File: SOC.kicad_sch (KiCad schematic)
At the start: 10 parts, among them J3 TF01-A, J4 CL24CR492, P1 HRO-TYPE-C-31-M-12, SW2 TS-1157-X-A, SW3 TS-1157-X-A, SW4 TS-1157-X-A, SW5 TS-1157-X-A, SW6 TS-1157-X-A, U12 W25Q128JVSIQ, U13 F1C200S

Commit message: dfdfasfasf
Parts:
- removed U13: F1C200S, rlib_ic:QFN-88_EP_10x10_Pitch0.4mm, symbol rlib_ic:F1C200S
- added C47, C48, C49, C50, C? (x12): 100n, symbol rlib_passive:C
- added R? (x4): R, symbol rlib_passive:R
- added U?: F1C200S, rlib_ic:QFN-88_EP_10x10_Pitch0.4mm, symbol rlib_ic:F1C200S
- U12: footprint Package_SO:SOIC-8_5.23x5.23mm_P1.27mm -> rlib_ic:SOIC-8_5.23x5.23mm_P1.27mm
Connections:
- net at SW3.1: now also SW3.2
- net at SW3.3 (K): now also SW3.4 (A)
- net at SW4.1: now also SW4.2
- net at SW4.3 (K): now also SW4.4 (A)
- net LCD_D0: now reaches J4.1 (DB0)
- net LCD_D0: now also U?.49 (PE0/CSI_HSYNC/LCD_D0/TWI2_SCK/TWI2_SCK/UART0_RX/EINTE0)
- net LCD_D1: now reaches J4.2 (DB1)
- net LCD_D1: now also U?.48 (PE1/CSI_VSYNC/LCD_D1/TWI2_SDA/UART0_TX/EINTE1)
- net LCD_D4: now reaches J4.22 (DB4)
- net LCD_D4: now also U?.8 (PD2/LCD_D4/UART1_CTS/EINTD2)
- net LCD_D8: now reaches J4.23 (DB8)
- net LCD_D8: now also U?.47 (PE2/CSI_PCLK/LCD_D8/CLK_OUT/EINTE2)
- net LCD_D9: now reaches J4.24 (DB9)
- net LCD_D9: now also U?.46 (PE3/CSI_D0/LCD_D9/DA_BCLK/RSB_SCK/EINTE3)
- net LCD_D10: now reaches J4.25 (DB10)
- net LCD_D10: now also U?.12 (PD6/LCD_D10/TWI1_SDA/EINTD6)
- net LCD_D12: now reaches J4.26 (DB11)
- net LCD_D12: now also J4.27 (DB12), U?.14 (PD8/LCD_D12/DA_BCLK/EINTD8)
- net LCD_D13: now reaches J4.28 (DB13)
- net LCD_D13: now also U?.15 (PD9/LCD_D13/DA_LRCK/EINTD9)
- net LCD_D14: now reaches J4.29 (DB14)
- net LCD_D14: now also U?.16 (PD10/LCD_D14/DA_IN/EINTD10)
- net LCD_D2: now reaches J4.3 (DB2)
- net LCD_D2: now also U?.6 (PD0/LCD_D2/TWI0_SDA/RSB_SDA/EINTD0)
- net LCD_D15: now reaches J4.30 (DB15)
- net LCD_D15: now also U?.17 (PD11/LCD_D15/DA_OUT/EINTD11)
- net GND: now reaches J4.34 (GND)
- net GND: now also J4.5 (GND), U12.4 (GND), C47.1, C48.2, C49.2, C50.2, C?.2, C?.2, C?.2, C?.2, C?.2, C?.2, C?.2, C?.2, C?.2, C?.2, C?.2, C?.2
- net LCD_D5: now reaches J4.35 (DB5)
- net LCD_D5: now also U?.9 (PD3/LCD_D5/UART1_RX/EINTD3)
- net LCD_D6: now reaches J4.36 (DB6)
- net LCD_D6: now also U?.10 (PD4/LCD_D6/UART1_TX/EINTD4)
- net LCD_D7: now reaches J4.37 (DB7)
- net LCD_D7: now also U?.11 (PD5/LCD_D7/TWI1_SCK/EINTD5)
- net LCD_D3: now reaches J4.4 (DB3)
- net LCD_D3: now also U?.7 (PD1/LCD_D3/UART1_RTS/EINTD1)
- net at SW2.1: now also SW2.2
- net at SW2.3 (K): now also SW2.4 (A)
- net at SW6.1: now also SW6.2
- net at SW6.3 (K): now also SW6.4 (A)
- net at SW5.1: now also SW5.2
- net at SW5.3 (K): now also SW5.4 (A)
- net at P1.A1 (GND), P1.A12 (GND), P1.B1 (GND)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: now also P1.S1 (SHIELD)
- net +3V3: now reaches U12.8 (VCC)
- net +3V3: now also J3.4 (VDD), C47.2, C48.1, C49.1, C50.1, C?.1, C?.1, C?.1, C?.1, R?.1, R?.1, R?.1, R?.1, U?.5 (VCC-IO), U?.67 (UVCC)
- net at J3.1 (DAT2): now also R?.2
- net at J3.2 (DAT3/CD): now also R?.2
- net at J3.7 (DAT0): now also R?.2
- net at J3.8 (DAT1): now also R?.2
- new net +1V1: C?.1, C?.1, C?.1, U?.71 (VDD-CORE)
- new net +2V5: C?.1, C?.1, C?.1, C?.1, C?.1, U?.31 (VCC-DRAM)
- new net BTN1: U?.59 (PC0/SPI0_CLK/SDC1_CLK)
- new net BTN2: U?.60 (PC1/SPI0_CS/SDC1_CMD)
- new net BTN3: U?.61 (PC2/SPI0_MISO/SDC1_D0)
- new net BTN4: U?.62 (PC3/SPI0_MOSI/UART0_TX)
- new net DAC_I2C_SCLK: U?.23 (PD15/LCD_D21/UART2_RTS/TWI2_SCK/EINTD15)
- new net DAC_I2C_SDIN: U?.24 (PD16/LCD_D22/UART2_CTS/TWI2_SDA/EINTD16)
- new net DAC_I2S_BCLK: U?.66 (PA0/TPX1/DA_BCLK/UART1_RTS/SPI1_CS)
- new net DAC_I2S_DIN: U?.63 (PA3/TPY2/IR_RX/DA_OUT/UART1_TX/SPI1_MISO)
- new net DAC_I2S_LRCK: U?.65 (PA1/TPX2/DA_LRCK/UART1_CTS/SPI1_MOSI)
- new net KEYS: U?.79 (LRADC0)
- new net LCD_D11: U?.13 (PD7/LCD_D11/DA_MCLK/EINTD7)
- new net LCD_D16: U?.45 (PE4/CSI_D1/LCD_D16/DA_LRCK/RSB_SDA/EINTE4)
- new net SDC_CLK: U?.56 (PF2/SDC0_CLK/UART0_RX/EINTF2)
- new net SDC_CMD: U?.55 (PF3/SDC0_CMD/DBG_DO/EINTF3)
- new net SDC_D0: U?.57 (PF1/SDC0_D0/DBG_DI/EINTF1)
- new net SDC_D1: U?.58 (PF0/SDC0_D1/DBG_MS/IR_RX/EINTF0)
- new net SDC_D2: U?.53 (PF5/SDC0_D2/DBG_CK/PWM1/EINTF5)
- new net SDC_D3: U?.54 (PF4/SDC0_D3/UART0_TX/EINTF4)
- new net TERM_RX: U?.21 (PD14/LCD_D20/UART2_RX/EINTD14)
- new net TERM_TX: U?.19 (PD13/LCD_D19/UART2_TX/EINTD13)
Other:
- note added: "VCC-IO"
- moved on the sheet: J3, J4, P1, SW2, SW3, SW4, SW5, SW6, U12

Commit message: lradc schematic
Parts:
- added C?: 100n, symbol rlib_passive:C
- added R? (x7): R, symbol rlib_passive:R
- added SW? (x2): KLS7-TS3606, symbol rlib_buttons:KLS7-TS3606
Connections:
- net +3V3: now also R?.1
- net GND: now also J3.6 (VSS), SW2.3 (K), SW2.4 (A), SW3.3 (K), SW3.4 (A), SW4.3 (K), SW4.4 (A), SW5.3 (K), SW5.4 (A), SW6.3 (K), SW6.4 (A), C?.2, SW?.2, SW?.2
- net KEYS: now also SW3.1, SW3.2, R?.1, R?.2
- net SDC_CMD: now also J3.3 (CMD)
- net SDC_D0: now also J3.7 (DAT0), R?.2
- net SDC_D1: now also J3.8 (DAT1), R?.2
- net SDC_D2: now also J3.1 (DAT2), R?.2
- net SDC_D3: now also J3.2 (DAT3/CD), R?.2
- net at SW4.1, SW4.2: now also R?.1, R?.2
- net at SW2.1, SW2.2: now also R?.1, R?.2
- net at SW6.1, SW6.2: now also R?.1, R?.2
- net at SW5.1, SW5.2: now also R?.1, R?.2
- net BTN1: no longer names the net of U?.59 (PC0/SPI0_CLK/SDC1_CLK)
- net BTN2: no longer names the net of U?.60 (PC1/SPI0_CS/SDC1_CMD)
- net BTN3: no longer names the net of U?.61 (PC2/SPI0_MISO/SDC1_D0)
- net BTN4: no longer names the net of U?.62 (PC3/SPI0_MOSI/UART0_TX)
- new net: C?.1, R?.2, SW?.1
- new net: R?.1, R?.2, SW?.1
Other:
- note removed: "VCC-IO"
- moved on the sheet: C48, C49, C50, SW2, SW3, SW4, SW5, SW6

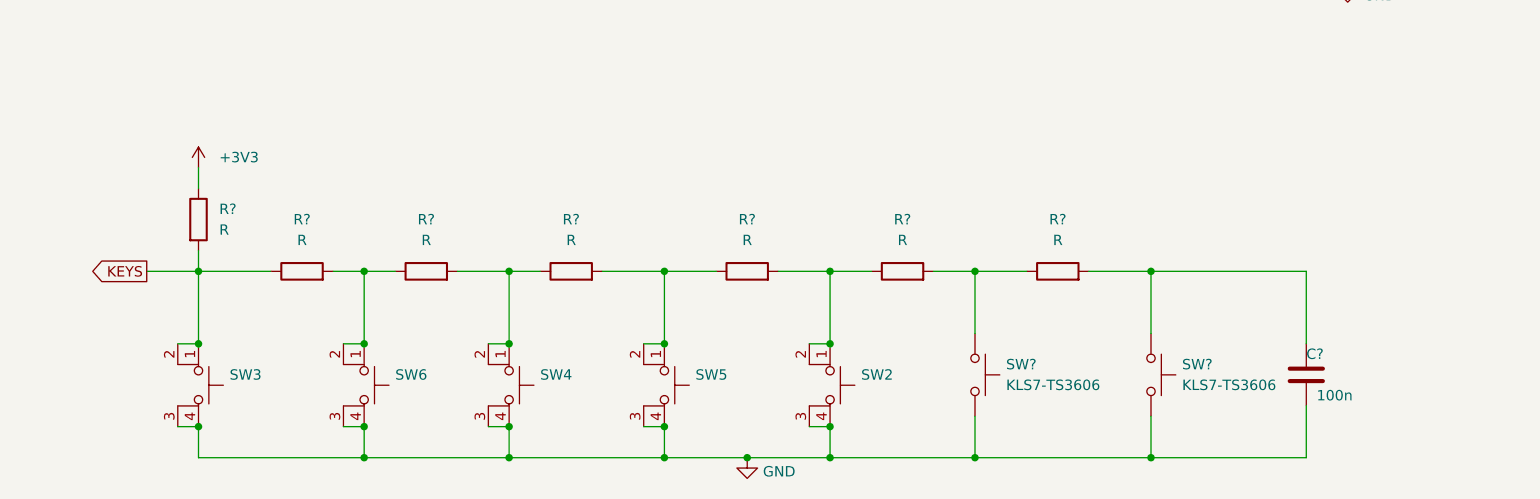
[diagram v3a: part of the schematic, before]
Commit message: changer inverted buck ic
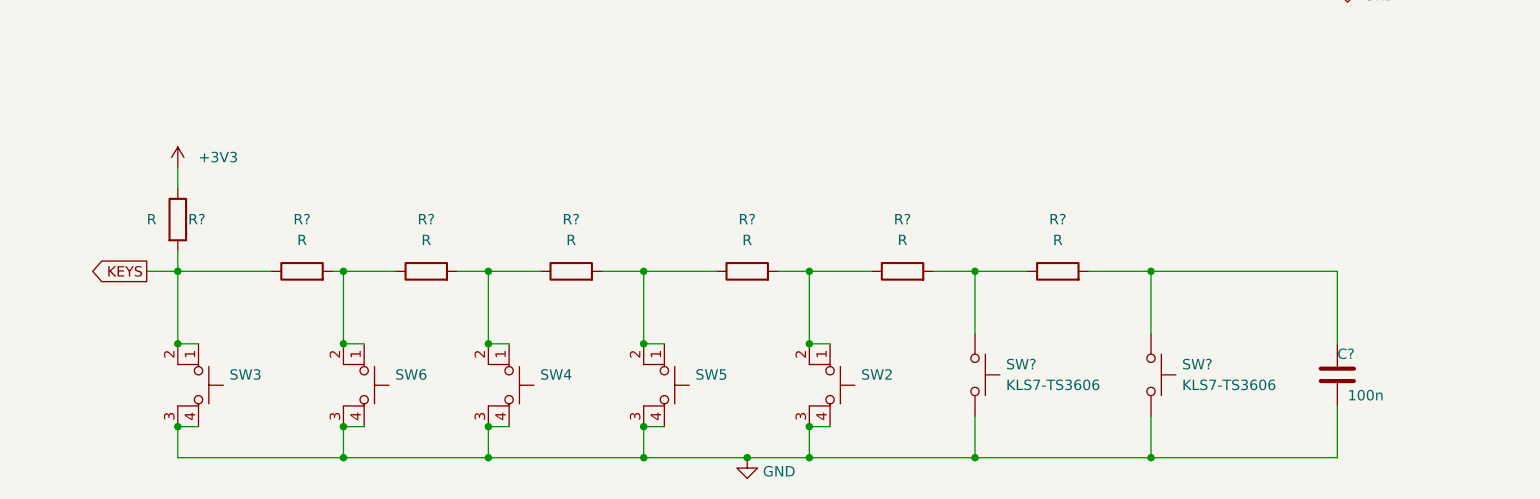
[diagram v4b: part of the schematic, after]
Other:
- moved on the sheet: C?, R?

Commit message: added winstar lcd
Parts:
- removed J4: CL24CR492, rlib_connectors:CL24CR92, symbol rlib_connectors:CL24CR492
- added C? (x3): 100n, symbol rlib_passive:C
- added P?: WF24HTLAJDNN0#, symbol rlib_lcd:WF24HTLAJDNN0#
- added R? (x2): R, symbol rlib_passive:R
- gave numbers to parts that had none: 27
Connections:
- net DAC_I2C_SDIN is gone; now on net DAC_I2C_SCLK: U4.24 (PD16/LCD_D22/UART2_CTS/TWI2_SDA/EINTD16)
- net +3V3: now also U12.3 (WP(IO2)), U12.7 (HOLD), C?.1, C?.1, P?.7 (VCC), P?.8 (IOVCC), R?.1, R?.1
- net DAC_I2C_SCLK: no longer U4.23 (PD15/LCD_D21/UART2_RTS/TWI2_SCK/EINTD15)
- net GND: now also J3.10 (SHIELD), P1.A1 (GND), P1.A12 (GND), P1.B1 (GND), P1.B12 (GND), P1.S1 (SHIELD), C?.2, C?.2, C?.2, P?.1 (GND), P?.38 (LEDA), P?.39 (GND)
- net LCD_D1: now also P?.15 (DB1)
- net LCD_D2: now also P?.16 (DB2)
- net SDC_CLK: now also J3.5 (CLX)
- net FLASH_SPI_MISO: now reaches U4.39 (PE10/CSI_D7/UART2_CTS/SPI1_MISO/EINTE10)
- net FLASH_SPI_MISO: now also U12.2 (DO(IO1))
- net FLASH_SPI_CLK: now reaches U4.40 (PE9/CSI_D6/UART2_RTS/SPI1_CLK/EINTE9)
- net FLASH_SPI_CLK: now also U12.6 (CLK)
- net FLASH_SPI_MOSI: now reaches U4.41 (PE8/CSI_D5/UART2_RX/SPI1_MOSI/EINTE8)
- net FLASH_SPI_MOSI: now also U12.5 (DI(IO0))
- net FLASH_SPI_CS: now reaches U4.42 (PE7/CSI_D4/UART2_TX/SPI1_CS/EINTE7)
- net FLASH_SPI_CS: now also U12.1 (CS), R?.2
- net LCD_PWM: now reaches U4.43 (PE6/CSI_D3/PWM1/DA_OUT/OWA_OUT/EINTE6)
- net at U4.70 (RESET): now also C?.1, R?.2
- new net: P?.34 (LEDK1), P?.35 (LEDK2), P?.36 (LEDK3), P?.37 (LEDK4)
- new net SOC_I2C_SCL: U4.23 (PD15/LCD_D21/UART2_RTS/TWI2_SCK/EINTD15)
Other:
- moved on the sheet: C47, C48, C49, C50, C54, C55, C56, C57, C58, C59, C60, C61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

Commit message: added crystal,backlight regulator and usb nets
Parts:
- added C68, C70, C71, C? (x2): 100n, symbol rlib_passive:C
- added C? (x2): 18p, symbol rlib_passive:C
- added JP1: SolderJumper_3_Open, symbol Jumper:SolderJumper_3_Open
- added L9: L, symbol rlib_passive:L
- added Q1: Q_NMOS_DSG, symbol Device:Q_NMOS_DSG
- added R38, R39, R40, R43, R44, R? (x2): R, symbol rlib_passive:R
- added U8: USBLC6-2SC6, Package_TO_SOT_SMD:SOT-23-6, symbol rlib_passive:USBLC6-2SC6
- added Y?: 24M, symbol Device:Crystal
- gave numbers to parts that had none: 6
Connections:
- net +1V1: now also U4.22 (VDD-CORE), U4.35 (VDD-CORE)
- net +2V5: now also U4.30 (VCC-DRAM), U4.32 (VCC-DRAM), U4.34 (VCC-DRAM), U4.36 (VCC-DRAM), C?.1, R?.1
- net +3V3: now also P2.30 (RESET), P2.34 (LEDK1), P2.35 (LEDK2), P2.36 (LEDK3), P2.37 (LEDK4), R41.2, U4.20 (VCC-IO), U4.50 (VCC-IO), JP1.1 (A); no longer R41.1
- net GND: now also P2.33 (GND), U4.82 (AGND), C68.2, C70.2, C71.2, C?.2, C?.2, C?.2, JP1.3 (B), Q1.2 (S), R39.2, R?.2, U8.2 (GND); no longer P2.38 (LEDA)
- net LCD_D0: now also P2.14 (DB0)
- net LCD_D10: now also P2.24 (DB10)
- net LCD_D11: now also P2.25 (DB11)
- net LCD_D12: now also P2.26 (DB12)
- net LCD_D13: now also P2.27 (DB13)
- net LCD_D14: now also P2.28 (DB14)
- net LCD_D15: now also P2.29 (DB15)
- net LCD_D3: now also P2.17 (DB3)
- net LCD_D4: now also P2.18 (DB4)
- net LCD_D5: now also P2.19 (DB5)
- net LCD_D6: now also P2.20 (DB6)
- net LCD_D7: now also P2.21 (DB7)
- net LCD_D8: now also P2.22 (DB8)
- net LCD_D9: now also P2.23 (DB9)
- net LCD_PWM: now also R40.2
- net LCD_CS: now reaches P2.10 (CS)
- net LCD_CS: now also U4.29 (PD21/LCD_VSYNC/SPI0_MISO/EINTD21)
- net LCD_RS: now reaches P2.11 (RS)
- net LCD_RS: now also U4.27 (PD19/LCD_DE/SPI0_MOSI/EINTD19)
- net LCD_WR: now reaches P2.12 (WR)
- net LCD_WR: now also U4.26 (PD18/LCD_CLK/SPI0_CS/EINTD18)
- net LCD_RD: now reaches P2.13 (RD)
- net LCD_RD: now also U4.28 (PD20/LCD_HSYNC/SPI0_CLK/EINTD20)
- net at P2.31 (IM0): now also JP1.2 (C)
- net at C69.1, U4.70 (RESET): now also R41.1; no longer R41.2
- net at U4.33 (SVREF): now also C?.1, C?.2, R?.1, R?.2
- net at U4.51 (HOSCI): now also C?.1, Y?.1
- net at U4.52 (HOSCO): now also C?.1, Y?.2
- net CHRG_IRQ: now reaches U4.59 (PC0/SPI0_CLK/SDC1_CLK)
- net AUDIO_PLUG: now reaches U4.60 (PC1/SPI0_CS/SDC1_CMD)
- net USB_D-: now reaches U4.68 (USB-DM)
- net USB_D-: now also R43.1
- net USB_D+: now reaches U4.69 (USB-DP)
- net USB_D+: now also R44.1
- net +3V0: now reaches U4.80 (AVCC)
- net +3V0: now also C68.1
- net at P1.A4 (VBUS), P1.A9 (VBUS), P1.B4 (VBUS)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: now also C71.1, L9.2
- net at P1.A6 (D+): now also U8.4 (I/O2)
- net at P1.A7 (D-): now also U8.6 (I/O1)
- net DAC_I2C_SCLK renamed SOC_I2C_SDA
- new net: R43.2, U8.1 (I/O1)
- new net: R44.2, U8.3 (I/O2)
- new net: P2.38 (LEDA), R38.1
- new net: Q1.1 (D), R38.2
- new net: Q1.3 (G), R39.1, R40.1
- new net VBUS: C70.1, L9.1, U8.5 (VBUS)
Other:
- note added: "BACKLIGHT"
- note added: "BUTTONS"
- note added: "FIRMWARE SPI FLASH"
- note added: "SD CARD"
- note added: "SOC"
- note added: "USB"
- moved on the sheet: C15, C47, C48, C49, C50, C54, C55, C56, C57, C58, C59, C60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

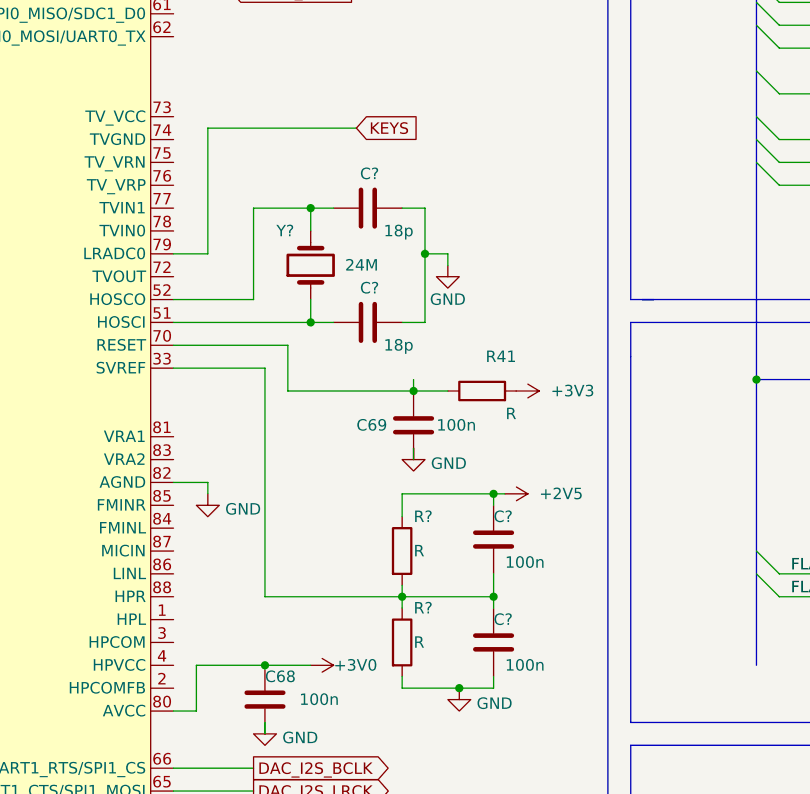
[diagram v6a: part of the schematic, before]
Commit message: changed volume buttons
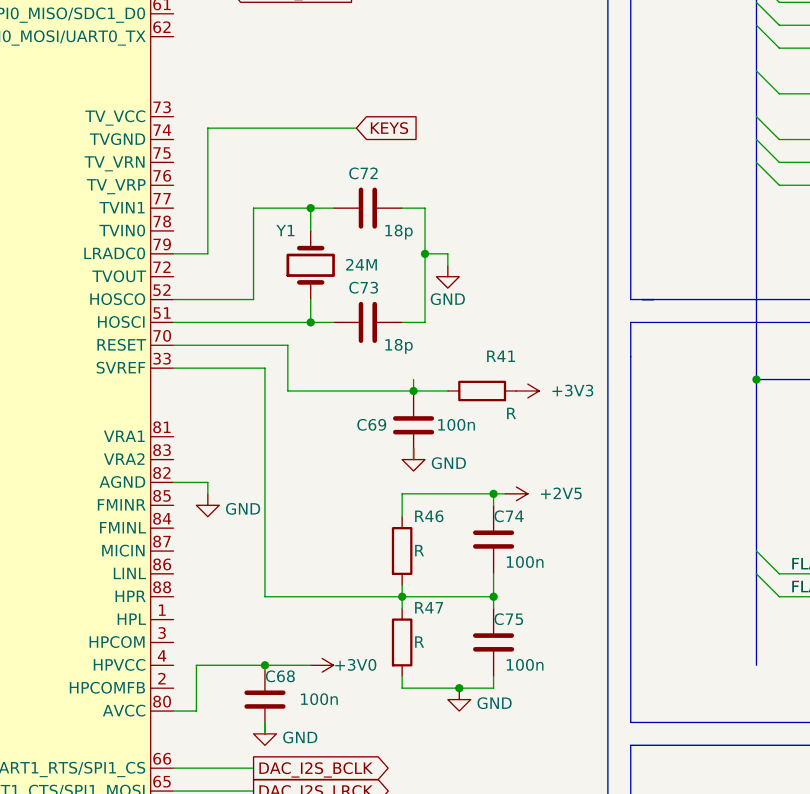
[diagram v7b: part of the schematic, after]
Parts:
- SW7, SW8: footprint (none) -> rlib_buttons:TS-1010-X-X; symbol rlib_buttons:KLS7-TS3606 -> rlib_buttons:TS-1010-C-A
- gave numbers to parts that had none: 7
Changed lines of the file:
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@@
   (symbol (lib_id "rlib_passive:C") (at 243.84 88.9 90) (unit 1)
     (in_bom yes) (on_board yes)
-    (property "Reference" "C?" (id 0) (at 245.11 85.09 90)
+    (property "Reference" "C73" (id 0) (at 245.11 85.09 90)
       (effects (font (size 1.27 1.27)) (justify left))
     )
@@
     (pin "2")
   )
-  (symbol (lib_id "rlib_buttons:KLS7-TS3606") (at 210.82 262.89 270) (unit 1)
+  (symbol (lib_id "rlib_buttons:TS-1010-C-A") (at 210.82 262.89 270) (unit 1)
     (in_bom yes) (on_board yes) (fields_autoplaced)
     (property "Reference" "SW8" (id 0) (at 214.63 261.6199 90)
@@
       (effects (font (size 1.27 1.27)) (justify left))
     )
-    (property "Footprint" "" (id 2) (at 215.9 262.89 0)
-      (effects (font (size 1.27 1.27)) hide)
-    )
-    (property "Datasheet" "${RLIB}/buttons/datasheets/KLS7-TS3606.pdf" (id 3) (at 215.9 262.89 0)
+    (property "Footprint" "rlib_buttons:TS-1010-X-X" (id 2) (at 205.74 261.62 0)
+      (effects (font (size 1.27 1.27)) hide)
+    )
+    (property "Datasheet" "${RLIB}/buttons/datasheets/TS-1010-C-A.pdf" (id 3) (at 215.9 262.89 0)
       (effects (font (size 1.27 1.27)) hide)
     )
@@
   (symbol (lib_id "rlib_passive:R") (at 247.65 124.46 0) (unit 1)
     (in_bom yes) (on_board yes)
-    (property "Reference" "R?" (id 0) (at 248.92 120.65 0)
+    (property "Reference" "R47" (id 0) (at 248.92 120.65 0)
       (effects (font (size 1.27 1.27)) (justify left))
     )
@@
   (symbol (lib_id "rlib_passive:C") (at 257.81 124.46 0) (unit 1)
     (in_bom yes) (on_board yes)
-    (property "Reference" "C?" (id 0) (at 257.81 121.92 0)
+    (property "Reference" "C75" (id 0) (at 257.81 121.92 0)
       (effects (font (size 1.27 1.27)) (justify left))
     )
@@
   (symbol (lib_id "rlib_passive:C") (at 257.81 113.03 0) (unit 1)
     (in_bom yes) (on_board yes)
-    (property "Reference" "C?" (id 0) (at 257.81 110.49 0)
+    (property "Reference" "C74" (id 0) (at 257.81 110.49 0)
       (effects (font (size 1.27 1.27)) (justify left))
     )
@@
   (symbol (lib_id "rlib_passive:R") (at 247.65 114.3 0) (unit 1)
     (in_bom yes) (on_board yes)
-    (property "Reference" "R?" (id 0) (at 248.92 110.49 0)
+    (property "Reference" "R46" (id 0) (at 248.92 110.49 0)
       (effects (font (size 1.27 1.27)) (justify left))
     )
@@
   (symbol (lib_id "rlib_passive:C") (at 243.84 76.2 90) (unit 1)
     (in_bom yes) (on_board yes)
-    (property "Reference" "C?" (id 0) (at 245.11 72.39 90)
+    (property "Reference" "C72" (id 0) (at 245.11 72.39 90)
       (effects (font (size 1.27 1.27)) (justify left))
     )
@@
   (symbol (lib_id "power:+2V5") (at 259.08 107.95 270) (unit 1)
     (in_bom yes) (on_board yes) (fields_autoplaced)
-    (property "Reference" "#PWR?" (id 0) (at 255.27 107.95 0)
+    (property "Reference" "#PWR0190" (id 0) (at 255.27 107.95 0)
       (effects (font (size 1.27 1.27)) hide)
     )
@@
   (symbol (lib_id "Device:Crystal") (at 237.49 82.55 90) (unit 1)
     (in_bom yes) (on_board yes)
-    (property "Reference" "Y?" (id 0) (at 233.68 78.74 90)
+    (property "Reference" "Y1" (id 0) (at 233.68 78.74 90)
       (effects (font (size 1.27 1.27)) (justify right))
     )
@@
   (symbol (lib_id "power:GND") (at 254 129.54 0) (unit 1)
     (in_bom yes) (on_board yes)
-    (property "Reference" "#PWR?" (id 0) (at 254 135.89 0)
+    (property "Reference" "#PWR0191" (id 0) (at 254 135.89 0)
       (effects (font (size 1.27 1.27)) hide)
     )
@@
   (symbol (lib_id "power:GND") (at 252.73 82.55 0) (unit 1)
     (in_bom yes) (on_board yes)
-    (property "Reference" "#PWR?" (id 0) (at 252.73 88.9 0)
+    (property "Reference" "#PWR0189" (id 0) (at 252.73 88.9 0)
       (effects (font (size 1.27 1.27)) hide)
     )
@@
     (pin "1")
   )
-  (symbol (lib_id "rlib_buttons:KLS7-TS3606") (at 189.23 262.89 270) (unit 1)
+  (symbol (lib_id "rlib_buttons:TS-1010-C-A") (at 189.23 262.89 270) (unit 1)
     (in_bom yes) (on_board yes) (fields_autoplaced)
     (property "Reference" "SW7" (id 0) (at 193.04 261.6199 90)
@@
       (effects (font (size 1.27 1.27)) (justify left))
     )
-    (property "Footprint" "" (id 2) (at 194.31 262.89 0)
-      (effects (font (size 1.27 1.27)) hide)
-    )
-    (property "Datasheet" "${RLIB}/buttons/datasheets/KLS7-TS3606.pdf" (id 3) (at 194.31 262.89 0)
-      (effects (font (size 1.27 1.27)) hide)
-    )
+    (property "Footprint" "rlib_buttons:TS-1010-X-X" (id 2) (at 184.15 261.62 0)
+      (effects (font (size 1.27 1.27)) hide)
+    )
+    (property "Datasheet" "${RLIB}/buttons/datasheets/TS-1010-C-A.pdf" (id 3) (at 194.31 262.89 0)
+      (effects (font (size 1.27 1.27)) hide)
+    )
